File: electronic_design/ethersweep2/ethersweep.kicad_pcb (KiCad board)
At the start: 2 copper layers, 60 x 60 mm, 20 parts, among them J1 Jack-DC, J2 ETH_LEFT, J3 ETH_RIGHT, J5 Conn_01x04_Female, M1 Stepper_Motor_bipolar

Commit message: raw component layout done
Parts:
- removed A1: Pololu_Breakout_DRV8825, Modules:Pololu_Breakout-16_15.2x20.3mm
- removed B1: ARDUINO_PRO_MINI, arduino_pro_mini:ARDUINO_PRO_MINI
- removed C100nF1: C, Capacitors_SMD:C_1206_HandSoldering
- removed C1_100uF1, C1_100uF2: CP, Capacitors_THT:CP_Radial_D8.0mm_P3.80mm
- removed C2_1uF1, C2_1uF2: CP, Capacitors_THT:CP_Radial_D5.0mm_P2.50mm
- removed the G*** at (110.4, 81.7)
- removed R1.66k1, R5k1: R, Resistors_SMD:R_0805_HandSoldering
- added C1: C100nF, Capacitor_SMD:C_0805_2012Metric, F.Cu at (166.5, 93.5)
- added C10: C22pF, Capacitor_SMD:C_0402_1005Metric, F.Cu at (174.5, 107.0)
- added C11: C22uF, Capacitor_Tantalum_SMD:CP_EIA-3216-12_Kemet-S, F.Cu at (189.5, 106.0)
- added C12: C100nF, Capacitor_SMD:C_0805_2012Metric, F.Cu at (179.5, 100.0)
- added C13: C1uF, Capacitor_SMD:C_0805_2012Metric, B.Cu at (127.5, 92.5)
- added C14: C1uF, Capacitor_SMD:C_0805_2012Metric, B.Cu at (139.0, 109.0)
- added C15: C1uF, Capacitor_SMD:C_0805_2012Metric, B.Cu at (132.0, 91.5)
- added C16: C1uF, Capacitor_SMD:C_0805_2012Metric, B.Cu at (147.0, 97.5)
- added C17: C1uF, Capacitor_SMD:C_0805_2012Metric, B.Cu at (147.0, 99.6)
- added C18: C10nF, Capacitor_SMD:C_0805_2012Metric, F.Cu at (198.5, 90.5)
- added C19: C100nF, Capacitor_SMD:C_0805_2012Metric, F.Cu at (193.5, 84.5)
- added C2: C22uF, Capacitor_Tantalum_SMD:CP_EIA-3216-12_Kemet-S, F.Cu at (189.0, 97.5)
- added C20: C100uF, Capacitor_SMD:CP_Elec_8x10, F.Cu at (196.0, 100.5)
- added C21: C0.47uF, Capacitor_SMD:C_0805_2012Metric, F.Cu at (184.0, 92.0)
- added C22: C100nF, Capacitor_SMD:C_0805_2012Metric, F.Cu at (198.5, 95.0)
- added C23: C100nF, Capacitor_SMD:C_0805_2012Metric, F.Cu at (198.5, 93.0)
- added C3: C1uF, Capacitor_SMD:C_0805_2012Metric, B.Cu at (126.0, 106.5)
- added C4: C22pF, Capacitor_SMD:C_0402_1005Metric, B.Cu at (134.5, 106.0)
- added C5: C22pF, Capacitor_SMD:C_0402_1005Metric, B.Cu at (128.5, 106.0)
- added C6: C100nF, Capacitor_SMD:C_0805_2012Metric, F.Cu at (188.5, 100.0)
- added C7: C1uF, Capacitor_SMD:C_0805_2012Metric, B.Cu at (126.0, 104.0)
- added C8: C22pF, Capacitor_SMD:C_0402_1005Metric, F.Cu at (168.6, 107.2)
- added C9: C100nF, Capacitor_SMD:C_0805_2012Metric, F.Cu at (188.9, 108.5)
- added H4: MountingHole_Pad, MountingHole:MountingHole_3.2mm_M3_Pad_Via, F.Cu at (167.0, 115.5)
- added H5: MountingHole_Pad, MountingHole:MountingHole_3.2mm_M3_Pad_Via, F.Cu at (124.5, 84.5)
- added H6: MountingHole_Pad, MountingHole:MountingHole_3.2mm_M3_Pad_Via, F.Cu at (155.5, 84.5)
- added H7: MountingHole_Pad, MountingHole:MountingHole_3.2mm_M3_Pad_Via, F.Cu at (155.5, 115.5)
- added H8: MountingHole_Pad, MountingHole:MountingHole_3.2mm_M3_Pad_Via, F.Cu at (124.5, 115.5)
- added J4: Conn_01x02_Male, Connector_JST:JST_EH_S2B-EH_1x02_P2.50mm_Horizontal, F.Cu at (131.5, 86.0)
- added J6: HR911105A, modules:HANRUN_HR911105A, F.Cu at (150.0, 100.0)
- added J7: Conn_01x04_Female, Connector_PinHeader_2.54mm:PinHeader_1x04_P2.54mm_Vertical, F.Cu at (172.5, 90.0)
- added J8: AVR-ISP-6, Connector_IDC:IDC-Header_2x03_P2.54mm_Vertical, B.Cu at (147.5, 87.5)
- added J9: Conn_01x04_Female, Connector_PinHeader_2.54mm:PinHeader_1x04_P2.54mm_Vertical, F.Cu at (150.0, 90.0)
- added R1: R5k, Resistor_SMD:R_0805_2012Metric, F.Cu at (180.0, 92.0)
- added R10: R1k, Resistor_SMD:R_0603_1608Metric, B.Cu at (136.0, 92.5)
- added R11: R200mOHM, Resistor_SMD:R_1206_3216Metric, F.Cu at (191.0, 84.0)
- added R12: R200mOHM, Resistor_SMD:R_1206_3216Metric, F.Cu at (188.5, 84.0)
- added R13: R330, Resistor_SMD:R_0603_1608Metric, B.Cu at (146.5, 113.5)
- added R2: R5k, Resistor_SMD:R_0805_2012Metric, F.Cu at (180.0, 90.0)
- added R3: R10k, Resistor_SMD:R_0805_2012Metric, B.Cu at (150.0, 111.5)
- added R4: R1k, Resistor_SMD:R_0603_1608Metric, B.Cu at (137.5, 92.5)
- added R5: R330, Resistor_SMD:R_0603_1608Metric, B.Cu at (151.5, 97.5)
- added R6: R330, Resistor_SMD:R_0603_1608Metric, B.Cu at (151.5, 99.5)
- added R7: R1k, Resistor_SMD:R_0603_1608Metric, B.Cu at (138.0, 106.5)
- added R8: R1k, Resistor_SMD:R_0603_1608Metric, B.Cu at (136.5, 106.5)
- added R9: R1k, Resistor_SMD:R_0603_1608Metric, B.Cu at (134.5, 92.5)
- added RV1: R_POT_10K, Potentiometer_THT:Potentiometer_Bourns_3296W_Vertical, F.Cu at (175.0, 112.0)
- added RX1: TestPoint, TestPoint:TestPoint_Pad_D2.0mm, B.Cu at (165.0, 108.0)
- added SW1: SW_Push, Button_Switch_SMD:SW_Push_SPST_NO_Alps_SKRK, B.Cu at (150.0, 115.5)
- added TX1: TestPoint, TestPoint:TestPoint_Pad_D2.0mm, B.Cu at (165.0, 104.9)
- added U1: ENC28J60x-SS, Package_SO:SSOP-28_5.3x10.2mm_P0.65mm, B.Cu at (133.0, 99.5)
- added U2: ATmega328-AU, Package_QFP:TQFP-32_7x7mm_P0.8mm, F.Cu at (171.5, 99.5)
- added U3: DRV8825PWPR, modules:IC_TPS61196PWPRQ1, F.Cu at (190.5, 92.0)
- added U4: AMS1117-3.3, Package_TO_SOT_SMD:SOT-223-3_TabPin2, F.Cu at (196.5, 108.5)
- added U5: AS5600, modules:AS5600, B.Cu at (182.5, 100.0)
- added Y1: Crystal_25MHz, Crystal:Crystal_SMD_3225-4Pin_3.2x2.5mm, B.Cu at (131.5, 106.5)
- added Y2: Crystal_8MHz, Crystal:Crystal_SMD_3225-4Pin_3.2x2.5mm, F.Cu at (171.5, 107.0)
- D1: value WS2812B -> LED; footprint LEDs:LED_WS2812B-PLCC4 -> LED_SMD:LED_0805_2012Metric; moved to B.Cu
- H1, H2, H3: value Mount -> MountingHole_Pad; footprint Mounting_Holes:MountingHole_3.5mm_Pad_Via -> MountingHole:MountingHole_3.2mm_M3_Pad_Via
- J1: value Jack-DC -> AVR-ISP-6; footprint Connectors:Barrel_Jack_CUI_PJ-036AH-SMT -> Connector_IDC:IDC-Header_2x03_P2.54mm_Vertical
- J2: value ETH_LEFT -> Conn_01x02_Male; footprint Pin_Headers:Pin_Header_Straight_1x08_Pitch2.54mm -> Connector_AMASS:AMASS_XT60-M_1x02_P7.20mm_Vertical
- J3: value ETH_RIGHT -> Conn_01x04_Female; footprint Pin_Headers:Pin_Header_Straight_1x08_Pitch2.54mm -> Connector_PinHeader_2.54mm:PinHeader_1x04_P2.54mm_Vertical; moved to B.Cu
- J5: value Conn_01x04_Female -> Conn_01x02_Male; footprint Pin_Headers:Pin_Header_Straight_1x04_Pitch2.54mm -> Connector_JST:JST_EH_S2B-EH_1x02_P2.50mm_Horizontal
- M1: footprint Pin_Headers:Pin_Header_Straight_1x04_Pitch2.54mm -> Connector_PinHeader_2.54mm:PinHeader_2x02_P2.54mm_Vertical_SMD
- moved H3 117.3 mm to (198.0, 115.5)
- moved J1 80.8 mm to (175.0, 87.5), turned to 180 degrees
- moved M1 71.3 mm to (182.5, 85.0), turned to 0 degrees
- moved J2 71.0 mm to (182.5, 114.5), turned to 0 degrees
- moved H2 70.6 mm to (198.0, 84.5)
- moved D1 35.3 mm to (146.5, 116.5), turned to 90 degrees
- moved H1 28.7 mm to (167.0, 84.5)
- moved J3 8.94 mm to (122.5, 96.0), turned to 180 degrees
- moved J5 7.76 mm to (139.5, 86.0)
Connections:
- D1 pad 1: +5V -> GND
- J1 pad 1: VCC -> MISO
- J1 pad 2: GND -> +3V3
- J1 pad 3: (no net) -> SCK
- J2 pad 1: +5V -> +12V
- J2 pad 2: +5V -> GND
- J3 pad 1: Net-(J3-Pad1) -> GND
- J3 pad 2: Net-(J3-Pad2) -> +3V3
- J3 pad 3: Net-(J3-Pad3) -> SCL
- J3 pad 4: Net-(B1-Pad15) -> SDA
- J5 pad 2: +5V -> ENDSTOP
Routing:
- net +5V: track 101.2 -> 0.00 mm
- net VCC: track 87.5 -> 0.00 mm
- net Net-(B1-Pad7): track 81.4 -> 0.00 mm
- net SCL: track 59.2 -> 0.00 mm, vias 1 -> 0
- net SDA: track 49.9 -> 0.00 mm, vias 1 -> 0
- net analog3: track 41.1 -> 0.00 mm
- net Net-(A1-Pad9): track 40.9 -> 0.00 mm
- net Net-(B1-Pad13): track 38.0 -> 0.00 mm, vias 1 -> 0
- net analog2: track 35.6 -> 0.00 mm
- net analog1: track 30.2 -> 0.00 mm
- net Net-(B1-Pad15): track 28.1 -> 0.00 mm, vias 1 -> 0
- net Net-(A1-Pad15): track 28.0 -> 0.00 mm
- net Net-(A1-Pad16): track 26.3 -> 0.00 mm
- net Net-(A1-Pad14): track 25.2 -> 0.00 mm
- net Net-(B1-Pad16): track 25.2 -> 0.00 mm, vias 1 -> 0
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- removed copper zone on B.Cu, net GND
- removed copper zone on F.Cu, net GND
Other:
- board size 60 x 60 mm -> 80.5 x 38 mm
- board text removed: "2020.02.23"
- board text removed: "ETHERNET CONTROLLER ENC28J60"
- board text removed: "OLED DISPLAY"
- board text removed: "github.com/neumi/ethersweep"

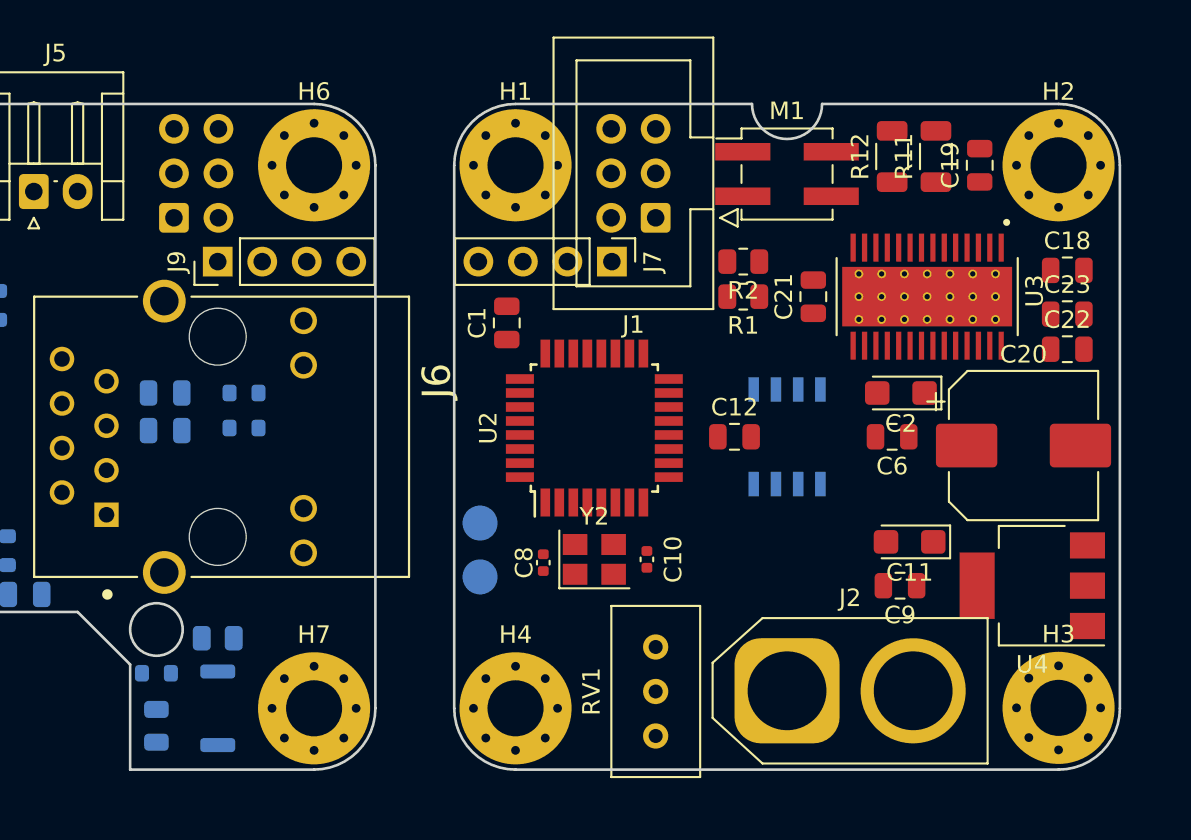
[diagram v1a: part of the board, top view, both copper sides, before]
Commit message: board layout and routing for 1st board done
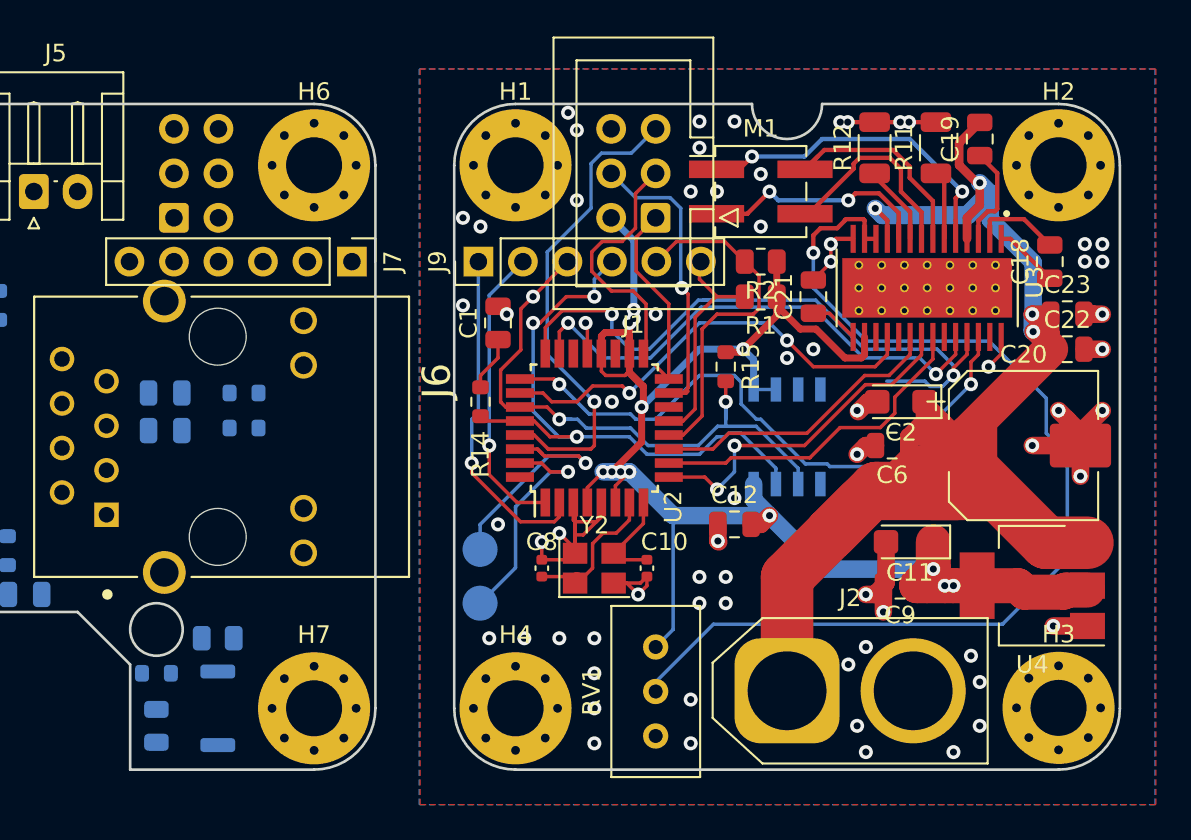
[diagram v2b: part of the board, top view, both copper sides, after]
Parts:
- added R14: R1k, Resistor_SMD:R_0603_1608Metric, F.Cu at (165.0, 98.0)
- added R15: R1k, Resistor_SMD:R_0603_1608Metric, F.Cu at (179.0, 96.0)
- J7: value Conn_01x04_Female -> Conn_01x06_Female; footprint Connector_PinHeader_2.54mm:PinHeader_1x04_P2.54mm_Vertical -> Connector_PinHeader_2.54mm:PinHeader_1x06_P2.54mm_Vertical
- J9: value Conn_01x04_Female -> Conn_01x06_Male; footprint Connector_PinHeader_2.54mm:PinHeader_1x04_P2.54mm_Vertical -> Connector_PinHeader_2.54mm:PinHeader_1x06_P2.54mm_Vertical
- moved J9 14.9 mm to (164.9, 90.0)
- moved J7 14.8 mm to (157.7, 90.0)
- moved C12 5.00 mm to (179.5, 105.0)
- moved M1 1.80 mm to (181.0, 86.0)
- moved C19 1.50 mm to (193.5, 83.0)
- moved RX1 1.50 mm to (165.0, 109.5)
- moved TX1 1.50 mm to (165.0, 106.4)
- moved C18 1.12 mm to (197.5, 90.0), turned to 90 degrees
- moved R12 1.12 mm to (187.5, 83.5)
- moved R1 1.00 mm to (181.0, 92.0)
- moved R2 1.00 mm to (181.0, 90.0)
- moved C1 0.50 mm to (166.0, 93.5)
- moved C10 0.50 mm to (174.5, 107.5)
- moved C2 0.50 mm to (189.0, 98.0)
- moved C6 0.50 mm to (188.5, 100.5)
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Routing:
- net +12V: track 0.00 -> 116.7 mm, vias 0 -> 4
- net +3V3: track 0.00 -> 110.0 mm, vias 0 -> 13
- net Net-(RV1-Pad2): track 0.00 -> 60.6 mm, vias 0 -> 1
- net GND: track 0.00 -> 57.5 mm, vias 0 -> 68
- net M1: track 0.00 -> 37.1 mm, vias 0 -> 2
- net M2: track 0.00 -> 35.4 mm, vias 0 -> 2
- net SDA: track 0.00 -> 35.1 mm, vias 0 -> 3
- net SCL: track 0.00 -> 34.7 mm, vias 0 -> 3
- net M0: track 0.00 -> 29.2 mm, vias 0 -> 2
- net rst: track 0.00 -> 27.4 mm, vias 0 -> 1
- net FLT_ETHERNET: track 0.00 -> 25.7 mm, vias 0 -> 2
- net ENDSTOP: track 0.00 -> 20.1 mm
- net STEPPER_ENABLE: track 0.00 -> 19.8 mm, vias 0 -> 2
- net STEP: track 0.00 -> 19.3 mm
- net RST_ETHERNET: track 0.00 -> 19.3 mm, vias 0 -> 1
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- added copper zone on B.Cu, net GND
- added copper zone on F.Cu, net GND

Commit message: board layouts done
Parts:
- moved C14 2.12 mm to (140.5, 107.5)
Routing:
- net +3V3: track 110.0 -> 219.5 mm
- net GND: track 57.5 -> 109.2 mm, vias 68 -> 149
- net SCL: track 34.7 -> 78.7 mm
- net SDA: track 35.1 -> 76.6 mm, vias 3 -> 6
- net rst: track 27.4 -> 67.6 mm, vias 1 -> 2
- net Net-(R5-Pad2): track 0.00 -> 35.6 mm, vias 0 -> 2
- net Net-(R6-Pad2): track 0.00 -> 34.5 mm, vias 0 -> 2
- net MOSI: track 17.6 -> 52.0 mm, vias 1 -> 2
- net Net-(C14-Pad1): track 0.00 -> 32.4 mm, vias 0 -> 7
- net ESTOP: track 12.7 -> 41.7 mm
- net SCK: track 14.8 -> 43.0 mm, vias 0 -> 1
- net MISO: track 11.5 -> 38.0 mm, vias 0 -> 1
- net CS_ETHERNET: track 16.8 -> 39.2 mm, vias 1 -> 2
- net RST_ETHERNET: track 19.3 -> 39.4 mm
- net ENDSTOP: track 20.1 -> 34.8 mm
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
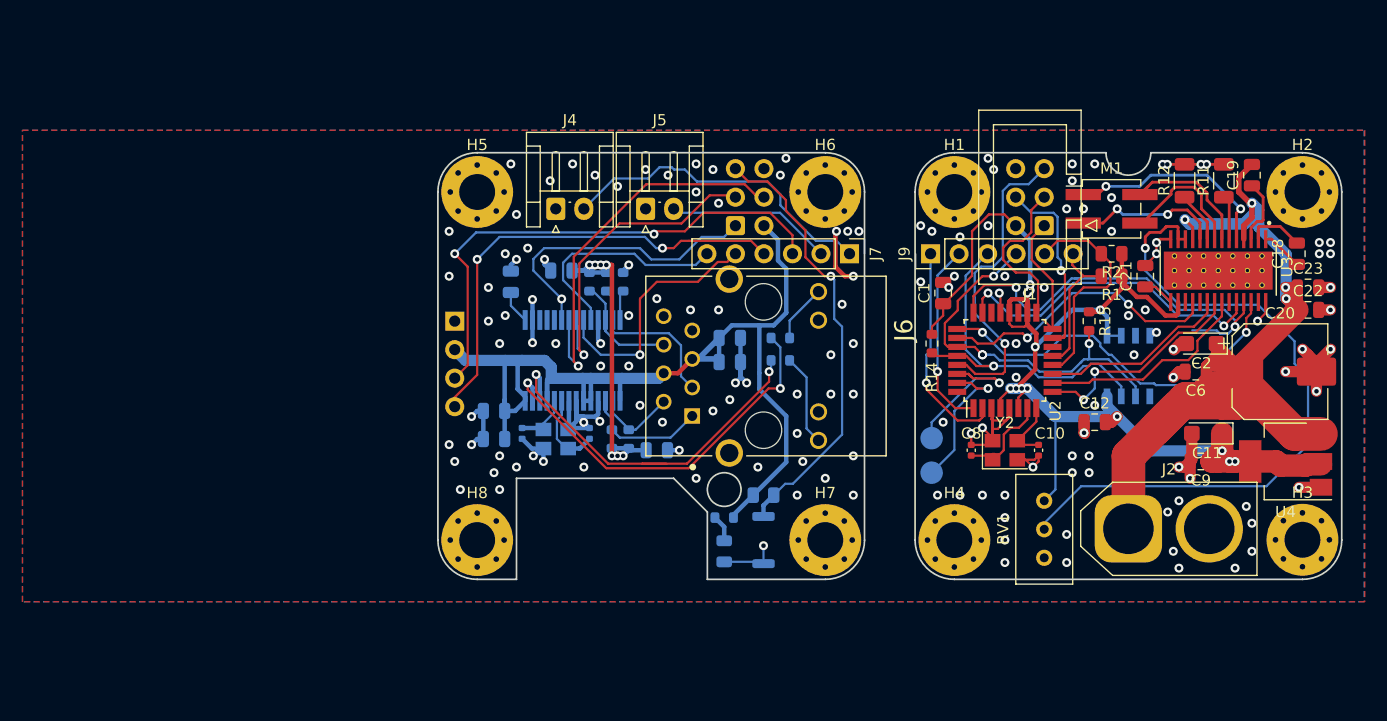
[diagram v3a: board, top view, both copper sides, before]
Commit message: board layout changed for single-piece manufacturing
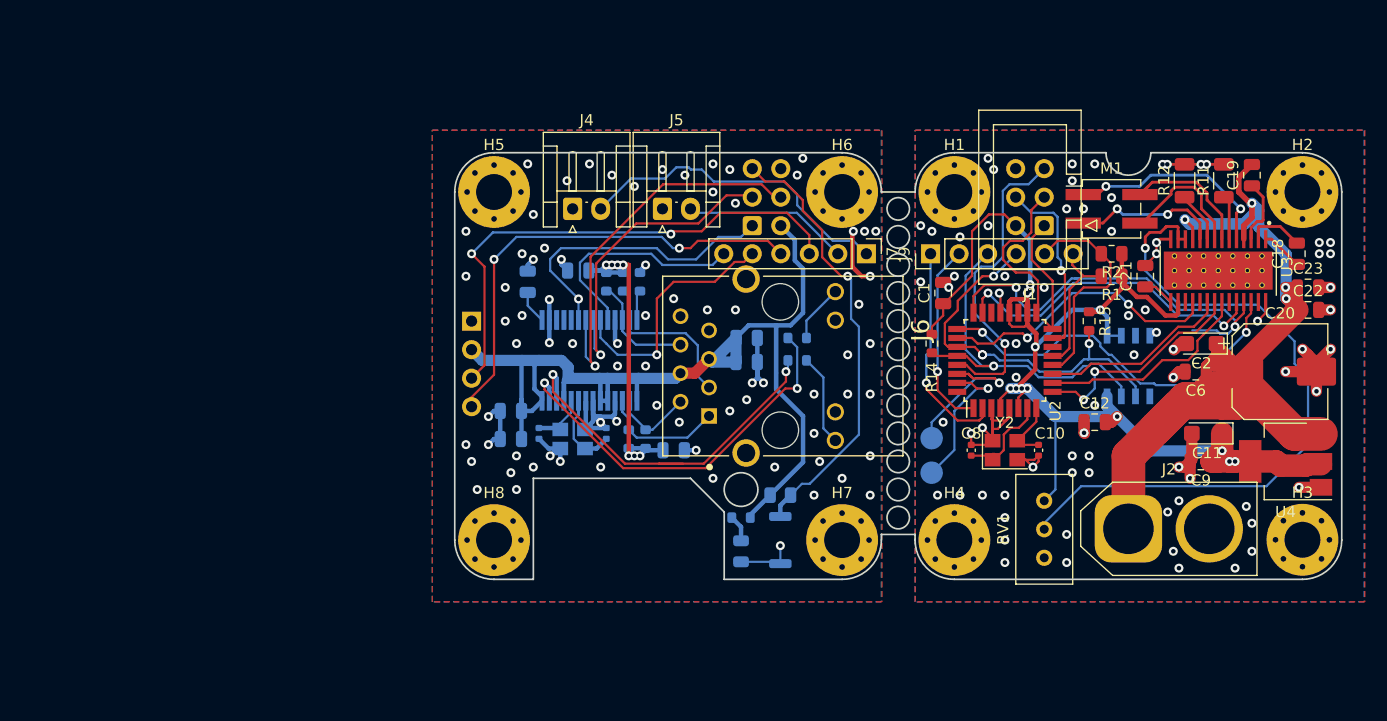
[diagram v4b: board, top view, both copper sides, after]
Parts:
- moved C13 1.50 mm to (129.0, 92.5)
- moved C14 1.50 mm to (142.0, 107.5)
- moved C15 1.50 mm to (133.5, 91.5)
- moved C16 1.50 mm to (148.5, 97.5)
- moved C17 1.50 mm to (148.5, 99.6)
- moved C3 1.50 mm to (127.5, 106.5)
- moved C4 1.50 mm to (136.0, 106.0)
- moved C5 1.50 mm to (130.0, 106.0)
- moved C7 1.50 mm to (127.5, 104.0)
- moved D1 1.50 mm to (148.0, 116.5)
- moved H5 1.50 mm to (126.0, 84.5)
- moved H6 1.50 mm to (157.0, 84.5)
- moved H7 1.50 mm to (157.0, 115.5)
- moved H8 1.50 mm to (126.0, 115.5)
- moved J3 1.50 mm to (124.0, 96.0)
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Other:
- board size 80.5 x 38 mm -> 79 x 38 mm

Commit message: small via fix
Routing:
- net MISO: vias 1 -> 0
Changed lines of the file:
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@@
   )
   (setup
-    (last_trace_width 1)
+    (last_trace_width 0.2)
     (user_trace_width 0.2)
     (user_trace_width 0.4)
@@
   (segment (start 168.7 93.763998) (end 168.7 95.25) (width 0.2) (layer F.Cu) (net 8))
   (segment (start 172.5 93) (end 172.299999 92.799999) (width 0.2) (layer F.Cu) (net 8))
-  (segment (start 170.75 98.25) (end 169.5 97) (width 0.2) (layer B.Cu) (net 9))
-  (segment (start 171.5 99) (end 170.75 98.25) (width 0.2) (layer B.Cu) (net 9))
-  (segment (start 176.700001 97.299999) (end 175 99) (width 0.2) (layer B.Cu) (net 9))
-  (segment (start 179.336001 97.299999) (end 176.700001 97.299999) (width 0.2) (layer B.Cu) (net 9))
-  (segment (start 180.754977 98.999979) (end 179.994999 98.240001) (width 0.2) (layer B.Cu) (net 9))
-  (segment (start 179.994999 97.958997) (end 179.336001 97.299999) (width 0.2) (layer B.Cu) (net 9))
-  (segment (start 183.550001 101.550001) (end 180.999979 98.999979) (width 0.2) (layer B.Cu) (net 9))
-  (segment (start 184.795003 101.550001) (end 183.550001 101.550001) (width 0.2) (layer B.Cu) (net 9))
-  (segment (start 179.994999 98.240001) (end 179.994999 97.958997) (width 0.2) (layer B.Cu) (net 9))
-  (segment (start 184.945003 101.700001) (end 184.795003 101.550001) (width 0.2) (layer B.Cu) (net 9))
-  (segment (start 175 99) (end 171.5 99) (width 0.2) (layer B.Cu) (net 9))
-  (segment (start 180.999979 98.999979) (end 180.754977 98.999979) (width 0.2) (layer B.Cu) (net 9))
-  (segment (start 188.299999 101.700001) (end 184.945003 101.700001) (width 0.2) (layer B.Cu) (net 9))
-  (segment (start 193 97) (end 188.299999 101.700001) (width 0.2) (layer B.Cu) (net 9))
+  (segment (start 186.200001 101.700001) (end 188.299999 101.700001) (width 0.2) (layer B.Cu) (net 9))
+  (segment (start 186.199999 101.699999) (end 186.200001 101.700001) (width 0.2) (layer B.Cu) (net 9))
+  (segment (start 179.336001 97.299999) (end 179.700001 97.663999) (width 0.2) (layer B.Cu) (net 9))
+  (segment (start 180.054999 98.300001) (end 180.200699 98.300001) (width 0.2) (layer B.Cu) (net 9))
+  (segment (start 188.299999 101.700001) (end 193 97) (width 0.2) (layer B.Cu) (net 9))
+  (segment (start 179.700001 97.663999) (end 179.700001 97.945003) (width 0.2) (layer B.Cu) (net 9))
+  (segment (start 185.300001 101.699999) (end 186.199999 101.699999) (width 0.2) (layer B.Cu) (net 9))
+  (segment (start 176.700001 97.299999) (end 179.336001 97.299999) (width 0.2) (layer B.Cu) (net 9))
+  (segment (start 179.700001 97.945003) (end 180.054999 98.300001) (width 0.2) (layer B.Cu) (net 9))
+  (segment (start 183.300003 99.700001) (end 185.300001 101.699999) (width 0.2) (layer B.Cu) (net 9))
+  (segment (start 171.5 99) (end 175 99) (width 0.2) (layer B.Cu) (net 9))
+  (segment (start 175 99) (end 176.700001 97.299999) (width 0.2) (layer B.Cu) (net 9))
+  (segment (start 181.600699 99.700001) (end 183.300003 99.700001) (width 0.2) (layer B.Cu) (net 9))
+  (segment (start 180.200699 98.300001) (end 181.600699 99.700001) (width 0.2) (layer B.Cu) (net 9))
+  (segment (start 169.5 97) (end 171.5 99) (width 0.2) (layer B.Cu) (net 9))
   (segment (start 188.65001 98.652824) (end 188.65001 97.738988) (width 0.2) (layer F.Cu) (net 11))
   (segment (start 190.825 95.563998) (end 190.825 94.3) (width 0.2) (layer F.Cu) (net 11))
@@
   (segment (start 133.525 95.9) (end 133.525 94.025) (width 0.2) (layer B.Cu) (net 17))
   (segment (start 133.525 94.025) (end 133.525 94.025) (width 0.2) (layer B.Cu) (net 17))
-  (via (at 133.525 94.025) (size 0.8) (drill 0.4) (layers F.Cu B.Cu) (net 17))
   (segment (start 146 88.5) (end 148 88.5) (width 0.2) (layer B.Cu) (net 17))
   (segment (start 140.5 89.5) (end 141.5 90.5) (width 0.2) (layer B.Cu) (net 17))
@@
   (segment (start 156.917998 92) (end 157.5 92) (width 0.2) (layer F.Cu) (net 19))
   (segment (start 157.5 92) (end 157.5 92) (width 0.2) (layer F.Cu) (net 19))
-  (via (at 157.5 92) (size 0.8) (drill 0.4) (layers F.Cu B.Cu) (net 19) (status 1000000))
+  (via (at 157.5 92) (size 0.8) (drill 0.4) (layers F.Cu B.Cu) (net 19))
   (segment (start 176.850001 97.215001) (end 176.850001 91.850001) (width 0.2) (layer F.Cu) (net 20))
   (segment (start 176.565002 97.5) (end 176.850001 97.215001) (width 0.2) (layer F.Cu) (net 20))
